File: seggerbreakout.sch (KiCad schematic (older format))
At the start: 0 parts

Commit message: Add footprints
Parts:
- added P?: JTAG, ~, symbol JTAG
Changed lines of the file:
@@
 LIBS:contrib
 LIBS:valves
+LIBS:seggerbreakout
+LIBS:seggerbreakout-cache
 EELAYER 27 0
 EELAYER END
@@
 Comment4 ""
 $EndDescr
+$Comp
+L JTAG P?
+U 1 1 532B5952
+P 4300 3500
+F 0 "P?" H 4300 4050 60  0001 C CNN
+F 1 "JTAG" H 4300 2950 60  0001 C CNN
+F 2 "~" H 4200 3550 60  0000 C CNN
+F 3 "~" H 4200 3550 60  0000 C CNN
+	1    4300 3500
+	1    0    0    -1
+$EndComp
 $EndSCHEMATC

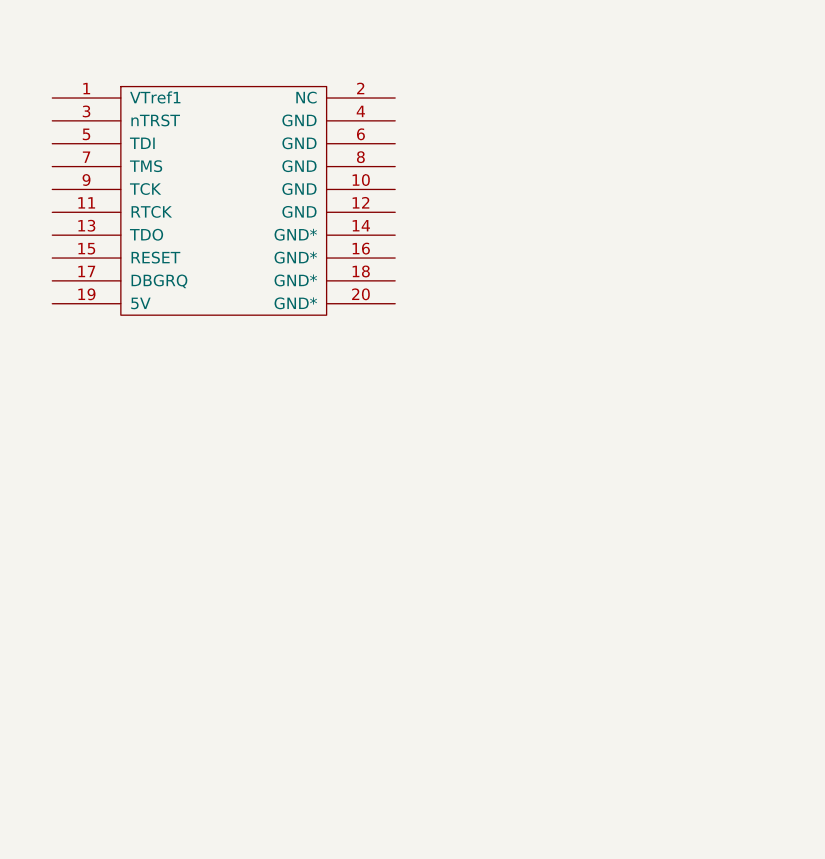
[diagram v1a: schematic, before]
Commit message: Add swd
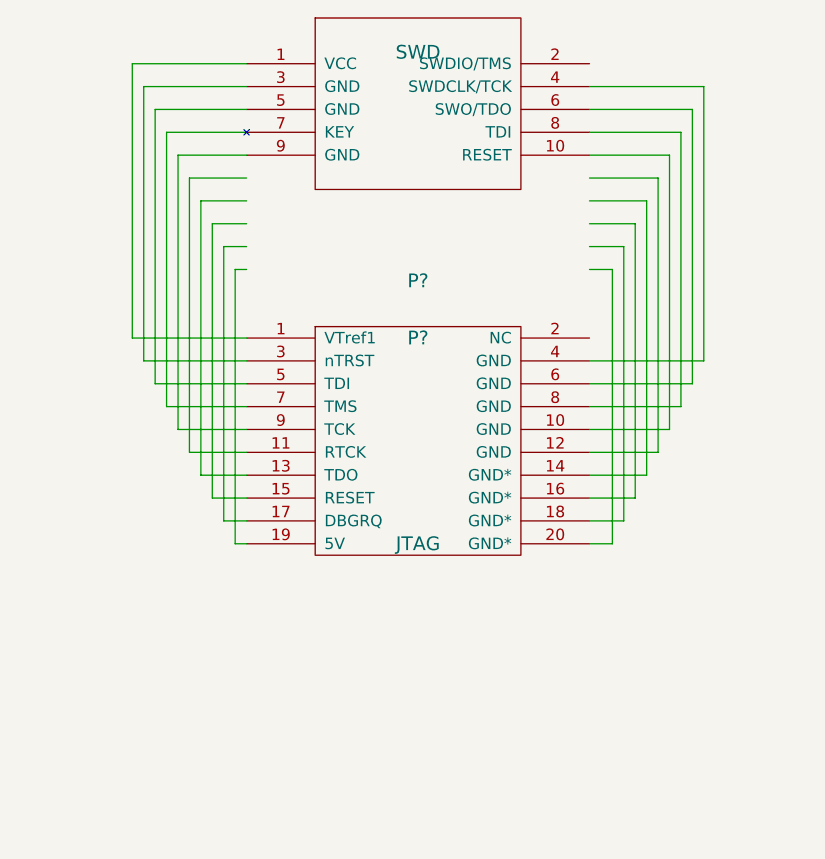
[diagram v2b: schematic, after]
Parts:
- added P?: SWD, ~, symbol SWD
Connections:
- wire segments 0 -> 57
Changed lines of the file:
@@
 Sheet 1 1
 Title ""
-Date "20 mar 2014"
+Date "24 mar 2014"
 Rev ""
 Comp ""
@@
 L JTAG P?
 U 1 1 532B5952
-P 4300 3500
-F 0 "P?" H 4300 4050 60  0001 C CNN
-F 1 "JTAG" H 4300 2950 60  0001 C CNN
-F 2 "~" H 4200 3550 60  0000 C CNN
-F 3 "~" H 4200 3550 60  0000 C CNN
-	1    4300 3500
+P 5150 4550
+F 0 "P?" H 5150 5000 60  0000 C CNN
+F 1 "JTAG" H 5150 4100 60  0000 C CNN
+F 2 "~" H 5050 4600 60  0000 C CNN
+F 3 "~" H 5050 4600 60  0000 C CNN
+	1    5150 4550
 	1    0    0    -1
 $EndComp
+$Comp
+L SWD P?
+U 1 1 532F6FA2
+P 5150 3300
+F 0 "P?" H 5150 2750 60  0000 C CNN
+F 1 "SWD" H 5150 3750 60  0000 C CNN
+F 2 "~" H 5150 3300 60  0000 C CNN
+F 3 "~" H 5150 3300 60  0000 C CNN
+	1    5150 3300
+	1    0    0    -1
+$EndComp
+Wire Wire Line
+	4400 5000 4350 5000
+Wire Wire Line
+	4350 5000 4350 3800
+Wire Wire Line
+	4350 3800 4400 3800
+Wire Wire Line
+	4400 3700 4300 3700
+Wire Wire Line
+	4300 3700 4300 4900
+Wire Wire Line
+	4300 4900 4400 4900
+Wire Wire Line
+	4400 3600 4250 3600
+Wire Wire Line
+	4250 3600 4250 4800
+Wire Wire Line
+	4250 4800 4400 4800
+Wire Wire Line
+	4400 3500 4200 3500
+Wire Wire Line
+	4200 3500 4200 4700
+Wire Wire Line
+	4200 4700 4400 4700
+Wire Wire Line
+	4400 3300 4100 3300
+Wire Wire Line
+	4100 3300 4100 4500
+Wire Wire Line
+	4100 4500 4400 4500
+Wire Wire Line
+	4400 3200 4050 3200
+Wire Wire Line
+	4050 3200 4050 4400
+Wire Wire Line
+	4050 4400 4400 4400
+Wire Wire Line
+	4400 3100 4000 3100
+Wire Wire Line
+	4000 3100 4000 4300
+Wire Wire Line
+	4000 4300 4400 4300
+Wire Wire Line
+	4400 3000 3950 3000
+Wire Wire Line
+	3950 3000 3950 4200
+Wire Wire Line
+	3950 4200 4400 4200
+Wire Wire Line
+	4400 2900 3900 2900
+Wire Wire Line
+	3900 2900 3900 4100
+Wire Wire Line
+	3900 4100 4400 4100
+Wire Wire Line
+	5900 3800 6000 3800
+Wire Wire Line
+	6000 3800 6000 5000
+Wire Wire Line
+	6000 5000 5900 5000
+Wire Wire Line
+	5900 4900 6050 4900
+Wire Wire Line
+	6050 4900 6050 3700
+Wire Wire Line
+	6050 3700 5900 3700
+Wire Wire Line
+	5900 4800 6100 4800
+Wire Wire Line
+	6100 4800 6100 3600
+Wire Wire Line
+	6100 3600 5900 3600
+Wire Wire Line
+	5900 4700 6150 4700
+Wire Wire Line
+	6150 4700 6150 3500
+Wire Wire Line
+	6150 3500 5900 3500
+Wire Wire Line
+	5900 4600 6200 4600
+Wire Wire Line
+	6200 4600 6200 3400
+Wire Wire Line
+	6200 3400 5900 3400
+Wire Wire Line
+	5900 4500 6250 4500
+Wire Wire Line
+	6250 4500 6250 3300
+Wire Wire Line
+	6250 3300 5900 3300
+Wire Wire Line
+	5900 4400 6300 4400
+Wire Wire Line
+	6300 4400 6300 3200
+Wire Wire Line
+	6300 3200 5900 3200
+Wire Wire Line
+	5900 4300 6350 4300
+Wire Wire Line
+	6350 4300 6350 3100
+Wire Wire Line
+	6350 3100 5900 3100
+Wire Wire Line
+	5900 4200 6400 4200
+Wire Wire Line
+	6400 4200 6400 3000
+Wire Wire Line
+	6400 3000 5900 3000
+Wire Wire Line
+	4400 3400 4150 3400
+Wire Wire Line
+	4150 3400 4150 4600
+Wire Wire Line
+	4150 4600 4400 4600
 $EndSCHEMATC

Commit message: Add a breakout portion for jtag connector
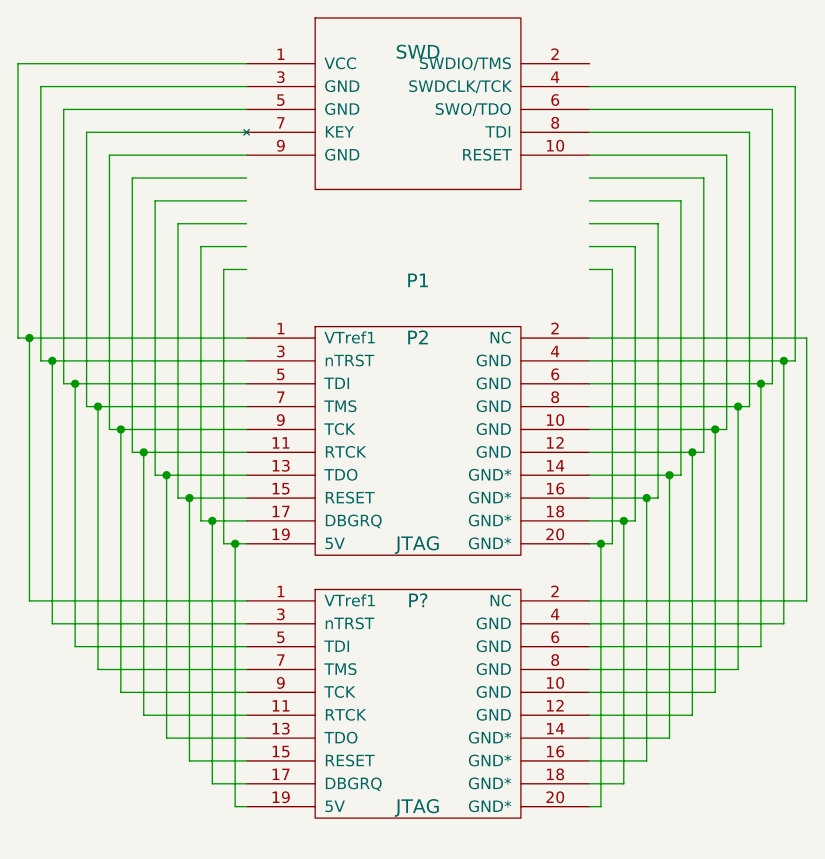
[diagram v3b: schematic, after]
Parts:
- added P?: JTAG, ~, symbol JTAG
- gave numbers to parts that had none: 2
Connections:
- wire segments 57 -> 98
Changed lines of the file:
@@
 Sheet 1 1
 Title ""
-Date "24 mar 2014"
+Date "18 apr 2014"
 Rev ""
 Comp ""
@@
 $EndDescr
 $Comp
-L JTAG P?
+L JTAG P2
 U 1 1 532B5952
 P 5150 4550
-F 0 "P?" H 5150 5000 60  0000 C CNN
+F 0 "P2" H 5150 5000 60  0000 C CNN
 F 1 "JTAG" H 5150 4100 60  0000 C CNN
 F 2 "~" H 5050 4600 60  0000 C CNN
@@
 $EndComp
 $Comp
-L SWD P?
+L SWD P1
 U 1 1 532F6FA2
 P 5150 3300
-F 0 "P?" H 5150 2750 60  0000 C CNN
+F 0 "P1" H 5150 2750 60  0000 C CNN
 F 1 "SWD" H 5150 3750 60  0000 C CNN
 F 2 "~" H 5150 3300 60  0000 C CNN
@@
 	1    0    0    -1
 $EndComp
-Wire Wire Line
-	4400 5000 4350 5000
-Wire Wire Line
-	4350 5000 4350 3800
-Wire Wire Line
-	4350 3800 4400 3800
-Wire Wire Line
-	4400 3700 4300 3700
-Wire Wire Line
-	4300 3700 4300 4900
-Wire Wire Line
-	4300 4900 4400 4900
-Wire Wire Line
-	4400 3600 4250 3600
-Wire Wire Line
-	4250 3600 4250 4800
-Wire Wire Line
-	4250 4800 4400 4800
-Wire Wire Line
-	4400 3500 4200 3500
-Wire Wire Line
-	4200 3500 4200 4700
-Wire Wire Line
-	4200 4700 4400 4700
-Wire Wire Line
-	4400 3300 4100 3300
-Wire Wire Line
-	4100 3300 4100 4500
-Wire Wire Line
-	4100 4500 4400 4500
-Wire Wire Line
-	4400 3200 4050 3200
-Wire Wire Line
-	4050 3200 4050 4400
-Wire Wire Line
-	4050 4400 4400 4400
-Wire Wire Line
-	4400 3100 4000 3100
-Wire Wire Line
-	4000 3100 4000 4300
-Wire Wire Line
-	4000 4300 4400 4300
-Wire Wire Line
-	4400 3000 3950 3000
-Wire Wire Line
-	3950 3000 3950 4200
-Wire Wire Line
-	3950 4200 4400 4200
-Wire Wire Line
-	4400 2900 3900 2900
-Wire Wire Line
-	3900 2900 3900 4100
-Wire Wire Line
-	3900 4100 4400 4100
+$Comp
+L JTAG P?
+U 1 1 53516C39
+P 5150 5700
+F 0 "P?" H 5150 6150 60  0000 C CNN
+F 1 "JTAG" H 5150 5250 60  0000 C CNN
+F 2 "~" H 5050 5750 60  0000 C CNN
+F 3 "~" H 5050 5750 60  0000 C CNN
+	1    5150 5700
+	1    0    0    -1
+$EndComp
+Wire Wire Line
+	4300 5000 4400 5000
+Wire Wire Line
+	4300 5000 4300 3800
+Wire Wire Line
+	4300 3800 4400 3800
+Wire Wire Line
+	4400 3700 4200 3700
+Wire Wire Line
+	4200 3700 4200 4900
+Wire Wire Line
+	4200 4900 4400 4900
+Wire Wire Line
+	4400 3600 4100 3600
+Wire Wire Line
+	4100 3600 4100 4800
+Wire Wire Line
+	4100 4800 4400 4800
+Wire Wire Line
+	4400 3500 4000 3500
+Wire Wire Line
+	4000 3500 4000 4700
+Wire Wire Line
+	4000 4700 4400 4700
+Wire Wire Line
+	4400 3300 3800 3300
+Wire Wire Line
+	3800 3300 3800 4500
+Wire Wire Line
+	3800 4500 4400 4500
+Wire Wire Line
+	4400 3200 3700 3200
+Wire Wire Line
+	3700 3200 3700 4400
+Wire Wire Line
+	3700 4400 4400 4400
+Wire Wire Line
+	4400 3100 3600 3100
+Wire Wire Line
+	3600 3100 3600 4300
+Wire Wire Line
+	3600 4300 4400 4300
+Wire Wire Line
+	4400 3000 3500 3000
+Wire Wire Line
+	3500 3000 3500 4200
+Wire Wire Line
+	3500 4200 4400 4200
+Wire Wire Line
+	4400 2900 3400 2900
+Wire Wire Line
+	3400 2900 3400 4100
+Wire Wire Line
+	3400 4100 4400 4100
 Wire Wire Line
 	5900 3800 6000 3800
@@
 	6000 5000 5900 5000
 Wire Wire Line
-	5900 4900 6050 4900
-Wire Wire Line
-	6050 4900 6050 3700
-Wire Wire Line
-	6050 3700 5900 3700
-Wire Wire Line
-	5900 4800 6100 4800
-Wire Wire Line
-	6100 4800 6100 3600
-Wire Wire Line
-	6100 3600 5900 3600
-Wire Wire Line
-	5900 4700 6150 4700
-Wire Wire Line
-	6150 4700 6150 3500
-Wire Wire Line
-	6150 3500 5900 3500
-Wire Wire Line
-	5900 4600 6200 4600
-Wire Wire Line
-	6200 4600 6200 3400
-Wire Wire Line
-	6200 3400 5900 3400
-Wire Wire Line
-	5900 4500 6250 4500
-Wire Wire Line
-	6250 4500 6250 3300
-Wire Wire Line
-	6250 3300 5900 3300
-Wire Wire Line
-	5900 4400 6300 4400
-Wire Wire Line
-	6300 4400 6300 3200
-Wire Wire Line
-	6300 3200 5900 3200
-Wire Wire Line
-	5900 4300 6350 4300
-Wire Wire Line
-	6350 4300 6350 3100
-Wire Wire Line
-	6350 3100 5900 3100
-Wire Wire Line
-	5900 4200 6400 4200
-Wire Wire Line
-	6400 4200 6400 3000
-Wire Wire Line
-	6400 3000 5900 3000
-Wire Wire Line
-	4400 3400 4150 3400
-Wire Wire Line
-	4150 3400 4150 4600
-Wire Wire Line
-	4150 4600 4400 4600
+	5900 4900 6100 4900
+Wire Wire Line
+	6100 4900 6100 3700
+Wire Wire Line
+	6100 3700 5900 3700
+Wire Wire Line
+	5900 4800 6200 4800
+Wire Wire Line
+	6200 4800 6200 3600
+Wire Wire Line
+	6200 3600 5900 3600
+Wire Wire Line
+	5900 4700 6300 4700
+Wire Wire Line
+	6300 4700 6300 3500
+Wire Wire Line
+	6300 3500 5900 3500
+Wire Wire Line
+	5900 4600 6400 4600
+Wire Wire Line
+	6400 4600 6400 3400
+Wire Wire Line
+	6400 3400 5900 3400
+Wire Wire Line
+	5900 4500 6500 4500
+Wire Wire Line
+	6500 4500 6500 3300
+Wire Wire Line
+	6500 3300 5900 3300
+Wire Wire Line
+	5900 4400 6600 4400
+Wire Wire Line
+	6600 4400 6600 3200
+Wire Wire Line
+	6600 3200 5900 3200
+Wire Wire Line
+	5900 4300 6700 4300
+Wire Wire Line
+	6700 4300 6700 3100
+Wire Wire Line
+	6700 3100 5900 3100
+Wire Wire Line
+	5900 4200 6800 4200
+Wire Wire Line
+	6800 4200 6800 3000
+Wire Wire Line
+	6800 3000 5900 3000
+Wire Wire Line
+	4400 3400 3900 3400
+Wire Wire Line
+	3900 3400 3900 4600
+Wire Wire Line
+	3900 4600 4400 4600
+Wire Wire Line
+	4350 5000 4350 6150
+Wire Wire Line
+	4350 6150 4400 6150
+Connection ~ 4350 5000
+Wire Wire Line
+	4250 4900 4250 6050
+Wire Wire Line
+	4250 6050 4400 6050
+Connection ~ 4250 4900
+Wire Wire Line
+	4150 4800 4150 5950
+Wire Wire Line
+	4150 5950 4400 5950
+Connection ~ 4150 4800
+Wire Wire Line
+	4050 4700 4050 5850
+Wire Wire Line
+	4050 5850 4400 5850
+Connection ~ 4050 4700
+Wire Wire Line
+	3950 4600 3950 5750
+Wire Wire Line
+	3950 5750 4400 5750
+Connection ~ 3950 4600
+Wire Wire Line
+	3850 4500 3850 5650
+Wire Wire Line
+	3850 5650 4400 5650
+Connection ~ 3850 4500
+Wire Wire Line
+	3750 4400 3750 5550
+Wire Wire Line
+	3750 5550 4400 5550
+Connection ~ 3750 4400
+Wire Wire Line
+	3650 4300 3650 5450
+Wire Wire Line
+	3650 5450 4400 5450
+Connection ~ 3650 4300
+Wire Wire Line
+	3550 4200 3550 5350
+Wire Wire Line
+	3550 5350 4400 5350
+Connection ~ 3550 4200
+Wire Wire Line
+	5950 5000 5950 6150
+Wire Wire Line
+	5950 6150 5900 6150
+Connection ~ 5950 5000
+Wire Wire Line
+	6050 4900 6050 6050
+Wire Wire Line
+	6050 6050 5900 6050
+Connection ~ 6050 4900
+Wire Wire Line
+	6150 4800 6150 5950
+Wire Wire Line
+	6150 5950 5900 5950
+Connection ~ 6150 4800
+Wire Wire Line
+	6250 4700 6250 5850
+Wire Wire Line
+	6250 5850 5900 5850
+Connection ~ 6250 4700
+Wire Wire Line
+	6350 4600 6350 5750
+Wire Wire Line
+	6350 5750 5900 5750
+Connection ~ 6350 4600
+Wire Wire Line
+	6450 4500 6450 5650
+Wire Wire Line
+	6450 5650 5900 5650
+Connection ~ 6450 4500
+Wire Wire Line
+	6550 4400 6550 5550
+Wire Wire Line
+	6550 5550 5900 5550
+Connection ~ 6550 4400
+Wire Wire Line
+	6650 4300 6650 5450
+Wire Wire Line
+	6650 5450 5900 5450
+Connection ~ 6650 4300
+Wire Wire Line
+	6750 4200 6750 5350
+Wire Wire Line
+	6750 5350 5900 5350
+Connection ~ 6750 4200
+Wire Wire Line
+	5900 4100 6850 4100
+Wire Wire Line
+	6850 4100 6850 5250
+Wire Wire Line
+	6850 5250 5900 5250
+Wire Wire Line
+	3450 4100 3450 5250
+Wire Wire Line
+	3450 5250 4400 5250
+Connection ~ 3450 4100
 $EndSCHEMATC
